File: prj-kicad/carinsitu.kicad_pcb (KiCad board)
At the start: 4 copper layers, 131.5 x 50 mm, 25 parts, among them P1 BAT, P2 MOT, U1 ESP32, U2 MIC2860, X1 40MHz

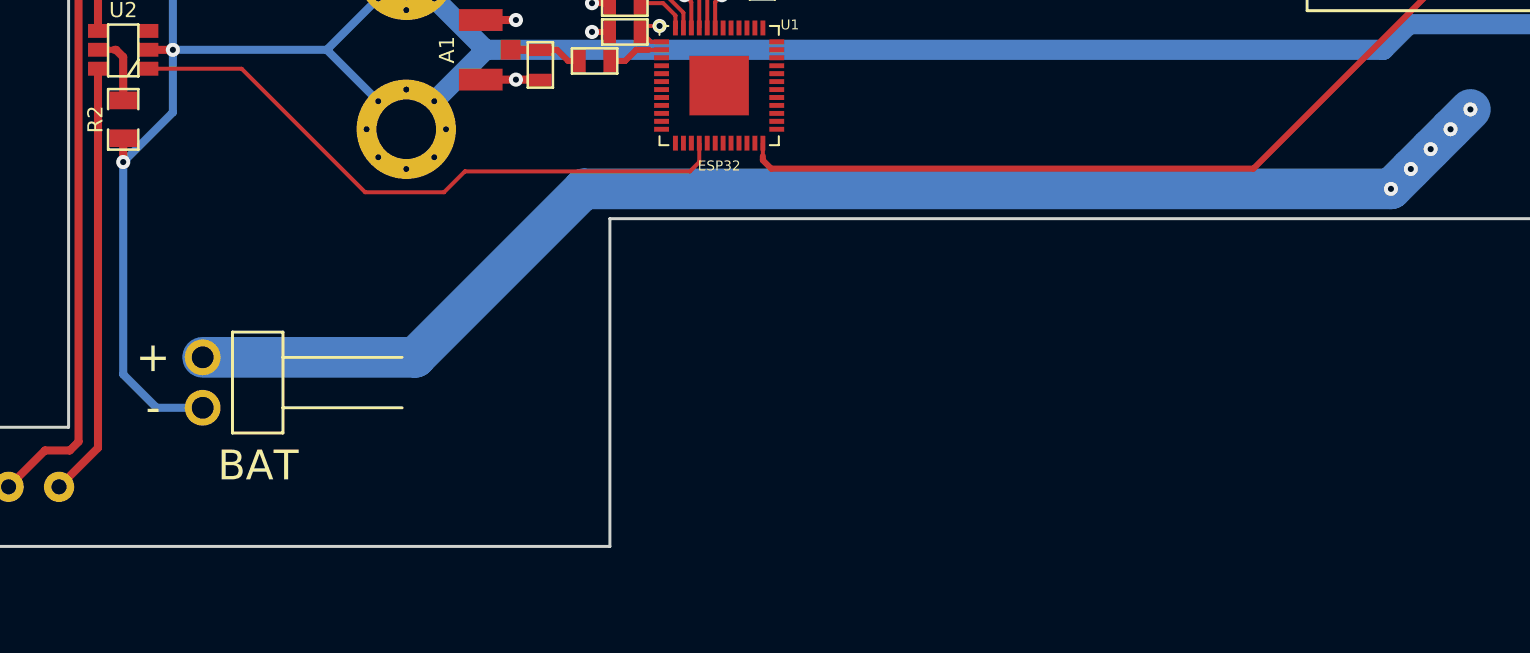
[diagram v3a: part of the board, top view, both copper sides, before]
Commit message: = ADD: Insert a slide switch to connect power (on / off)
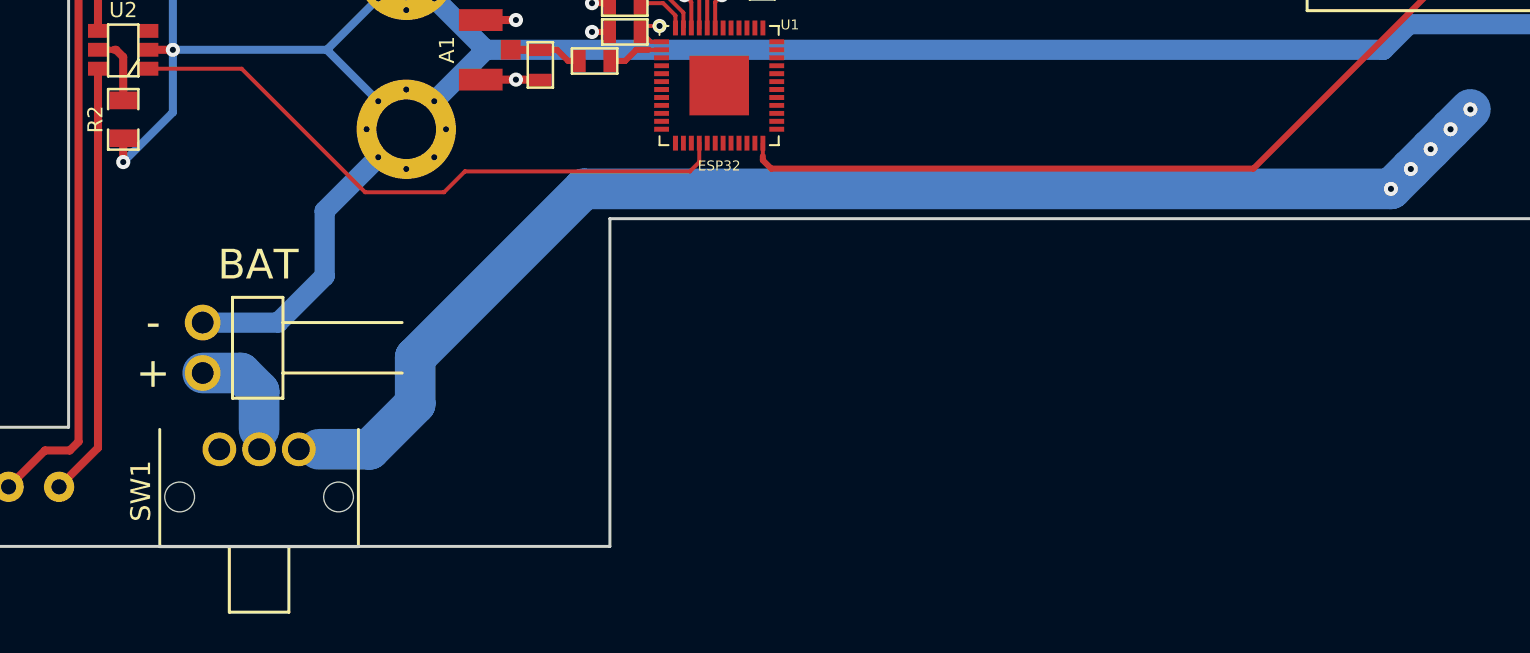
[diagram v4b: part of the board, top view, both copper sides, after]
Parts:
- added SW1: SWITCH_SLIDE, carinsitu:SW_L102xxxML, F.Cu at (95.3, 125.1)
- moved P1 1.75 mm to (94.5, 120.0)
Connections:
- P1 pad 1: GND -> Net-(P1-Pad1)
- P1 pad 2: Net-(MOD1-Pad4) -> GND
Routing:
- net Net-(P1-Pad1): track 0.00 -> 6.14 mm
- net Net-(MOD1-Pad4): track 101.7 -> 100.2 mm
- net GND: track 276.5 -> 277.3 mm
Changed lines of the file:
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@@
 (kicad_pcb (version 4) (host pcbnew 4.0.2+dfsg1-stable)
   (general
-    (links 88)
+    (links 89)
     (no_connects 5)
-    (area 73.750001 78.949999 214.315001 133.950001)
+    (area 82.674999 79.924999 214.315001 130.075001)
     (thickness 1.6)
     (drawings 27)
-    (tracks 173)
+    (tracks 181)
     (zones 0)
-    (modules 25)
-    (nets 56)
+    (modules 26)
+    (nets 58)
   )
   (page A4)
@@
   (layers
     (0 F.Cu signal)
-    (1 In1.Cu signal hide)
+    (1 In1.Cu signal)
     (2 In2.Cu signal)
-    (31 B.Cu signal hide)
+    (31 B.Cu signal)
     (32 B.Adhes user)
     (33 F.Adhes user)
@@
   )
   (setup
-    (last_trace_width 0.2032)
+    (last_trace_width 1.016)
     (user_trace_width 0.2032)
     (user_trace_width 0.3048)
@@
   (net 54 "Net-(U1-Pad41)")
   (net 55 "Net-(U1-Pad42)")
+  (net 56 "Net-(P1-Pad1)")
+  (net 57 "Net-(SW1-Pad1)")
   (net_class Default "This is the default net class."
     (clearance 0.1524)
@@
     (add_net "Net-(MOD1-Pad5)")
     (add_net "Net-(MOD1-Pad6)")
+    (add_net "Net-(P1-Pad1)")
     (add_net "Net-(R2-Pad2)")
+    (add_net "Net-(SW1-Pad1)")
     (add_net "Net-(U1-Pad10)")
     (add_net "Net-(U1-Pad11)")
@@
   )
   (module carinsitu:CONN_61300211021 locked (layer F.Cu)
-    (at 94.5 121.75 90)
+    (at 94.5 120 90)
     (fp_text reference P1 (at 0 1.05 90) (layer F.SilkS) hide
       (effects (font (size 0.5 0.5) (thickness 0.125)))
     )
-    (fp_text value BAT (at -4.18 2.79 180) (layer F.SilkS)
+    (fp_text value BAT (at 4.18 2.79 180) (layer F.SilkS)
       (effects (font (size 1.5 1.5) (thickness 0.2032)))
     )
@@
     (fp_line (start -2.54 4.04) (end -2.54 1.5) (layer F.SilkS) (width 0.15))
     (pad 1 thru_hole circle (at -1.27 0 90) (size 1.8 1.8) (drill 1.1) (layers *.Cu *.Mask)
-      (net 1 GND))
+      (net 56 "Net-(P1-Pad1)"))
     (pad 2 thru_hole circle (at 1.27 0 90) (size 1.8 1.8) (drill 1.1) (layers *.Cu *.Mask F.SilkS)
-      (net 7 "Net-(MOD1-Pad4)"))
+      (net 1 GND))
   )
   (module carinsitu:ESC (layer F.Cu)
@@
     )
   )
-  (gr_text + (at 92 120.48) (layer F.SilkS)
+  (module carinsitu:SW_L102xxxML (layer F.Cu)
+    (at 95.34 125.11)
+    (fp_text reference SW1 (at -3.95 2.1 90) (layer F.SilkS)
+      (effects (font (size 1 1) (thickness 0.15)))
+    )
+    (fp_text value SWITCH_SLIDE (at 2 2.4) (layer F.Fab)
+      (effects (font (size 0.5 0.5) (thickness 0.1016)))
+    )
+    (fp_line (start 0.5 4.9) (end 0.5 8.2) (layer F.SilkS) (width 0.15))
+    (fp_line (start 0.5 8.2) (end 3.5 8.2) (layer F.SilkS) (width 0.15))
+    (fp_line (start 3.5 8.2) (end 3.5 4.9) (layer F.SilkS) (width 0.15))
+    (fp_line (start 7 -1) (end 7 4.9) (layer F.SilkS) (width 0.15))
+    (fp_line (start 7 4.9) (end -3 4.9) (layer F.SilkS) (width 0.15))
+    (fp_line (start -3 4.9) (end -3 -1) (layer F.SilkS) (width 0.15))
+    (pad 1 thru_hole circle (at 0 0) (size 1.7 1.7) (drill 1.1) (layers *.Cu *.Mask)
+      (net 57 "Net-(SW1-Pad1)"))
+    (pad 2 thru_hole circle (at 2 0) (size 1.7 1.7) (drill 1.1) (layers *.Cu *.Mask)
+      (net 56 "Net-(P1-Pad1)"))
+    (pad 3 thru_hole circle (at 4 0) (size 1.7 1.7) (drill 1.1) (layers *.Cu *.Mask)
+      (net 7 "Net-(MOD1-Pad4)"))
+    (pad "" np_thru_hole circle (at -2 2.4) (size 1.5 1.5) (drill 1.5) (layers *.Cu *.Mask))
+    (pad "" np_thru_hole circle (at 6 2.4) (size 1.5 1.5) (drill 1.5) (layers *.Cu *.Mask))
+  )
+  (gr_text + (at 92 121.27) (layer F.SilkS)
     (effects (font (size 1.5 1.5) (thickness 0.3)))
   )
-  (gr_text - (at 92 123.02) (layer F.SilkS)
+  (gr_text - (at 92.01 118.73) (layer F.SilkS)
     (effects (font (size 1.5 1.5) (thickness 0.3)))
   )
@@
   (gr_line (start 213.21 80) (end 214.24 82.48) (angle 90) (layer Edge.Cuts) (width 0.15))
   (gr_line (start 82.75 80) (end 213.21 80) (angle 90) (layer Edge.Cuts) (width 0.15))
+  (segment (start 94.5 118.73) (end 98.3 118.73) (width 1.016) (layer B.Cu) (net 1) (status 400000))
+  (segment (start 100.64 113.11) (end 104.75 109) (width 1.016) (layer B.Cu) (net 1) (status 800000))
+  (segment (start 100.64 116.39) (end 100.64 113.11) (width 1.016) (layer B.Cu) (net 1))
+  (segment (start 98.3 118.73) (end 100.64 116.39) (width 1.016) (layer B.Cu) (net 1))
   (segment (start 122.67 99.67) (end 122.67 100.44) (width 0.3048) (layer In2.Cu) (net 1))
   (segment (start 122.67 100.44) (end 122.11 101) (width 0.3048) (layer In2.Cu) (net 1))
@@
   (segment (start 148.83 89.2) (end 146.25 89.2) (width 2.048) (layer F.Cu) (net 1))
   (segment (start 154.17 83.86) (end 148.83 89.2) (width 2.048) (layer F.Cu) (net 1))
-  (segment (start 90.5 110.65) (end 90.5 121.34) (width 0.4064) (layer B.Cu) (net 1))
-  (segment (start 92.18 123.02) (end 94.5 123.02) (width 0.4064) (layer B.Cu) (net 1))
-  (segment (start 90.5 121.34) (end 92.18 123.02) (width 0.4064) (layer B.Cu) (net 1))
   (segment (start 93 108.15) (end 90.5 110.65) (width 0.4064) (layer B.Cu) (net 1))
   (segment (start 93 108.15) (end 93 105) (width 0.4064) (layer B.Cu) (net 1))
@@
   (segment (start 102.68 112.17) (end 96.4625 105.9525) (width 0.2032) (layer F.Cu) (net 6))
   (segment (start 96.4625 105.9525) (end 91.77 105.9525) (width 0.2032) (layer F.Cu) (net 6))
+  (segment (start 99.34 125.11) (end 100.34 125.11) (width 1.016) (layer B.Cu) (net 7) (status 400000))
+  (segment (start 105.2 122.82) (end 102.91 125.11) (width 2.048) (layer B.Cu) (net 7))
+  (segment (start 102.91 125.11) (end 100.34 125.11) (width 2.048) (layer B.Cu) (net 7))
+  (segment (start 113.68 112) (end 154.32 112) (width 2.048) (layer B.Cu) (net 7))
+  (segment (start 113.68 112) (end 105.2 120.48) (width 2.048) (layer B.Cu) (net 7))
+  (segment (start 105.2 120.48) (end 105.2 122.82) (width 2.048) (layer B.Cu) (net 7))
   (segment (start 155.32 111) (end 154.32 112) (width 2.048) (layer In1.Cu) (net 7))
   (segment (start 156.32 110) (end 155.32 111) (width 2.048) (layer In1.Cu) (net 7))
@@
   (segment (start 155.32 111) (end 154.32 112) (width 2.048) (layer B.Cu) (net 7))
   (via (at 154.32 112) (size 0.7112) (drill 0.3048) (layers F.Cu B.Cu) (net 7))
-  (segment (start 105.2 120.48) (end 94.5 120.48) (width 2.048) (layer B.Cu) (net 7))
-  (segment (start 113.68 112) (end 105.2 120.48) (width 2.048) (layer B.Cu) (net 7))
-  (segment (start 154.32 112) (end 113.68 112) (width 2.048) (layer B.Cu) (net 7))
   (segment (start 113.468 105.56) (end 112.9 105.56) (width 0.3048) (layer F.Cu) (net 10))
   (segment (start 112.9 105.56) (end 112.338 104.998) (width 0.3048) (layer F.Cu) (net 10))
@@
   (segment (start 116.33 105) (end 116.97 105) (width 0.3048) (layer F.Cu) (net 13))
   (segment (start 116.97 105) (end 117.6 105) (width 0.2032) (layer F.Cu) (net 13))
-  (segment (start 122.7 110.35) (end 122.7 109.7) (width 0.2032) (layer F.Cu) (net 14) (status 800000))
-  (segment (start 170.8 81.53) (end 170.8 87.58) (width 0.3048) (layer F.Cu) (net 14) (status 400000))
+  (segment (start 122.7 110.35) (end 122.7 109.7) (width 0.2032) (layer F.Cu) (net 14))
+  (segment (start 170.8 81.53) (end 170.8 87.58) (width 0.3048) (layer F.Cu) (net 14))
   (segment (start 170.8 87.58) (end 147.4 110.98) (width 0.3048) (layer F.Cu) (net 14))
   (segment (start 147.4 110.98) (end 123.12 110.98) (width 0.3048) (layer F.Cu) (net 14))
@@
   (segment (start 119.9 103.9) (end 119.9 100.1) (width 0.2032) (layer F.Cu) (net 26))
   (segment (start 119.9 100.1) (end 121 99) (width 0.2032) (layer F.Cu) (net 26))
+  (segment (start 97.34 125.11) (end 97.34 124.1) (width 1.016) (layer B.Cu) (net 56) (status 400000))
+  (segment (start 96.42 121.27) (end 97.34 122.19) (width 2.048) (layer B.Cu) (net 56))
+  (segment (start 97.34 122.19) (end 97.34 124.1) (width 2.048) (layer B.Cu) (net 56))
+  (segment (start 96.42 121.27) (end 94.5 121.27) (width 2.048) (layer B.Cu) (net 56) (status 800000))
 )

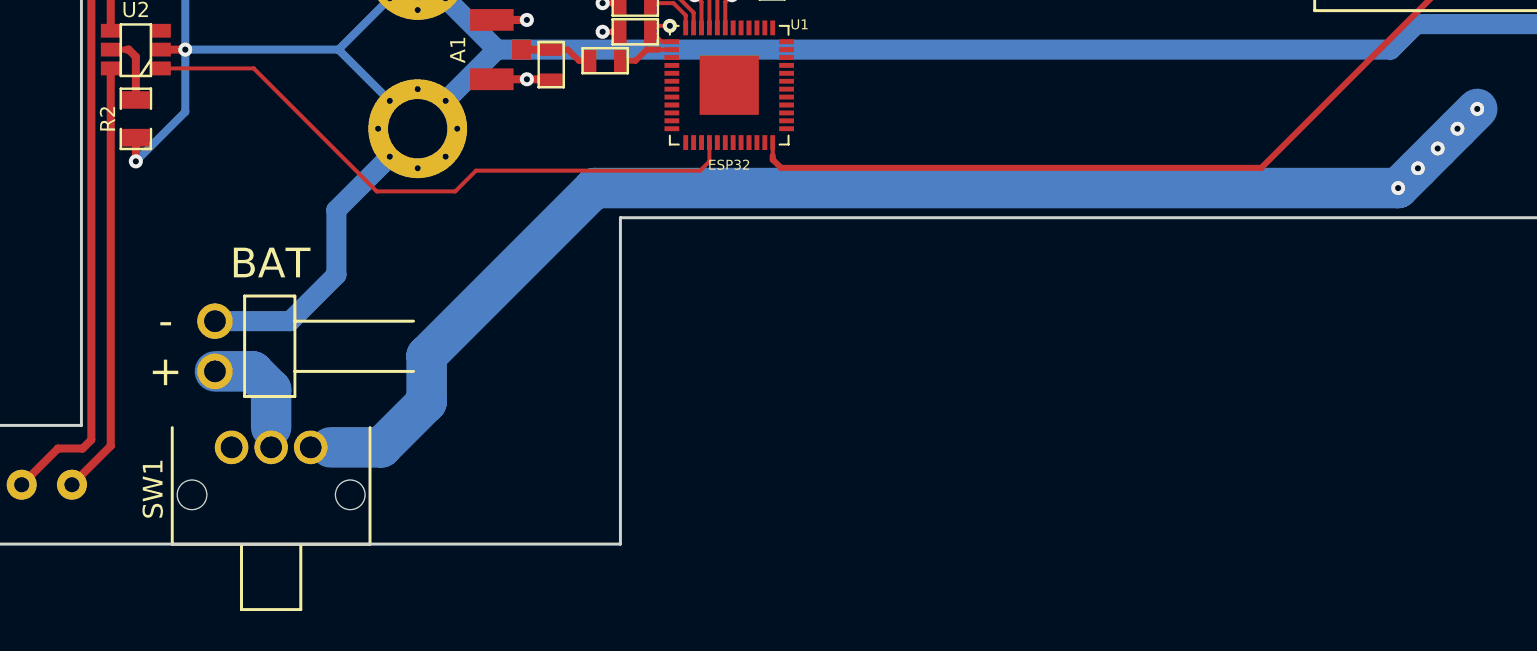
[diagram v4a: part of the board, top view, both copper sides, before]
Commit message: = ADD: Insert battery monitor (STC3100)
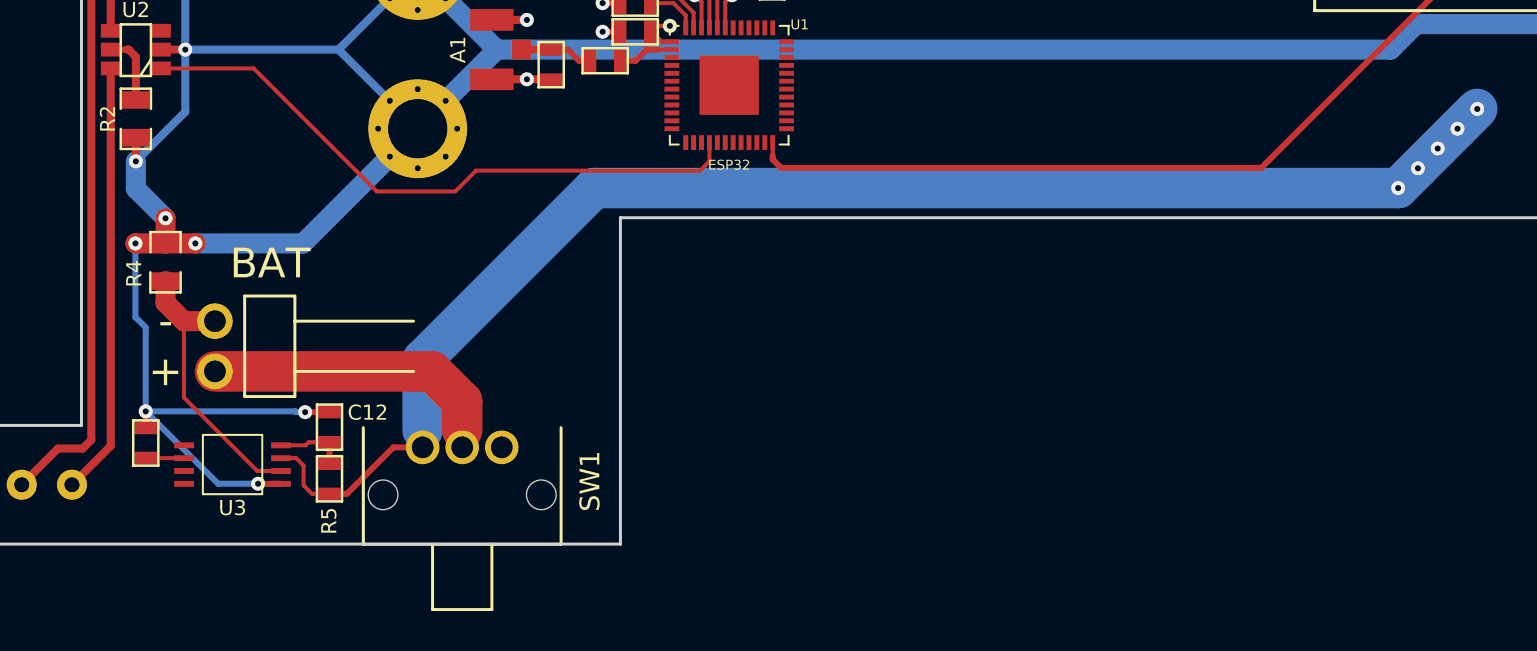
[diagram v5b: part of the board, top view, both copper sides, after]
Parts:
- added C12: 220nF, carinsitu:SMD0603, F.Cu at (100.3, 124.1)
- added R3: 200k, carinsitu:SMD0603, F.Cu at (91.0, 124.9)
- added R4: 0.01, carinsitu:SMD0805, F.Cu at (92.0, 115.8)
- added R5: 1k, carinsitu:SMD0603, F.Cu at (100.3, 126.7)
- added U3: STC3100, carinsitu:MSOP-8, F.Cu at (95.4, 126.0)
- moved SW1 9.66 mm to (105.0, 125.1)
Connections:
- MOD1 pad 4: Net-(MOD1-Pad4) -> +VBAT
- P1 pad 2: GND -> Net-(P1-Pad2)
- SW1 pad 1: Net-(SW1-Pad1) -> +VBAT
- SW1 pad 3: Net-(MOD1-Pad4) -> Net-(SW1-Pad3)
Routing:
- net +VBAT: track 0.00 -> 105.2 mm, vias 0 -> 5
- net Net-(MOD1-Pad4): track 100.2 -> 0.00 mm, vias 5 -> 0
- net GND: track 277.3 -> 309.8 mm, vias 11 -> 17
- net Net-(P1-Pad2): track 0.00 -> 14.3 mm
- net Net-(P1-Pad1): track 6.14 -> 15.4 mm
- net Net-(C12-Pad1): track 0.00 -> 3.60 mm
- net Net-(R3-Pad2): track 0.00 -> 1.94 mm
